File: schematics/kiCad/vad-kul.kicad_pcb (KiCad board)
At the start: 2 copper layers, 39 x 53.3 mm, 11 parts, among them J1 Lepton2Breakout, U1 RPIHeader

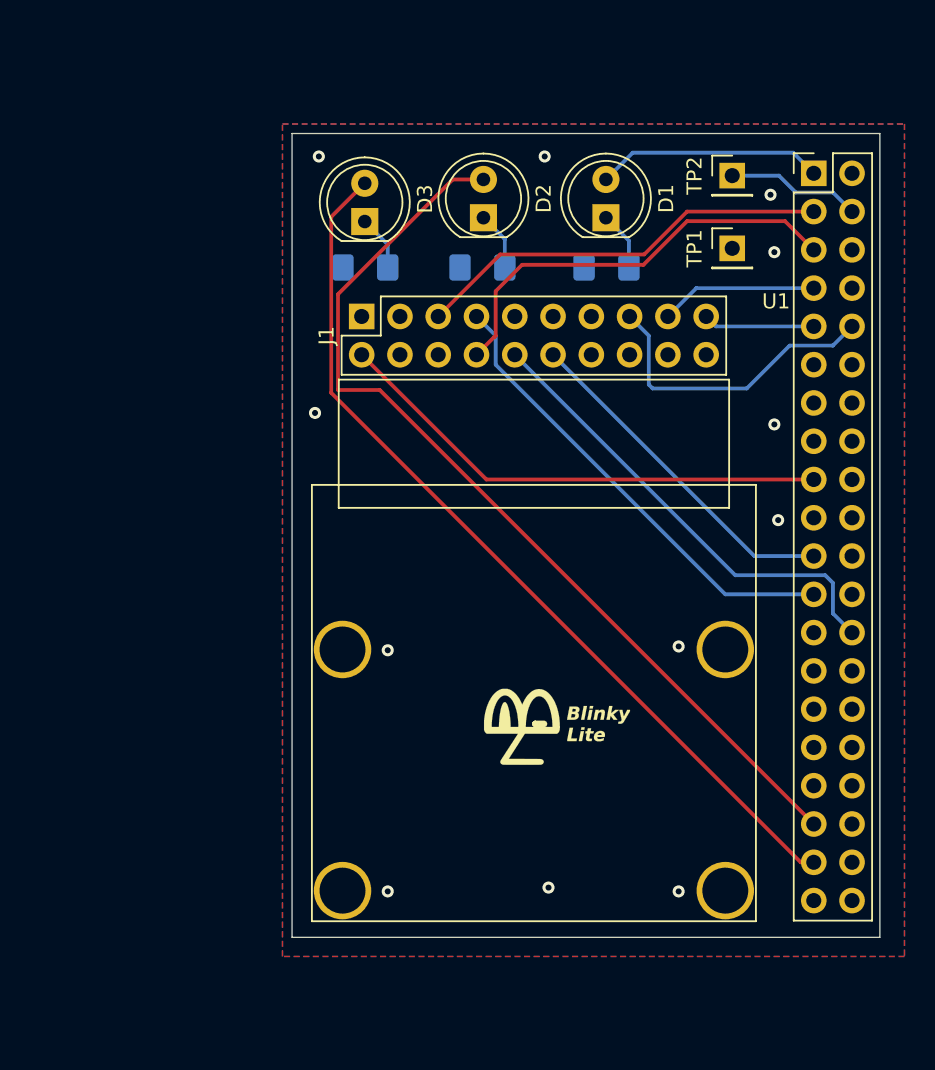
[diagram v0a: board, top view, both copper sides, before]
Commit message: new pcb with sr04
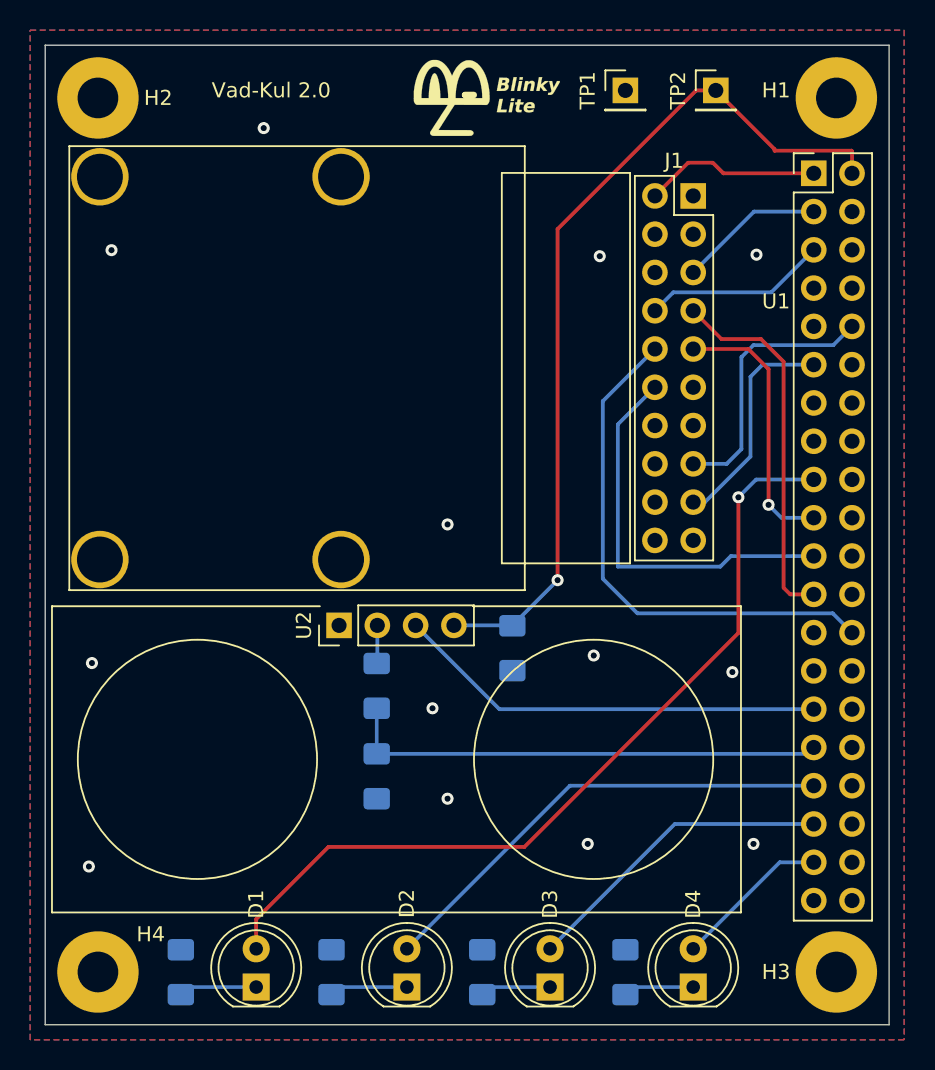
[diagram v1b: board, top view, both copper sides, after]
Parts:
- added C1: 1uF, Capacitor_SMD:C_1206_3216Metric_Pad1.42x1.75mm_HandSolder, B.Cu at (134.0, 57.0)
- added D4: LED, LED_THT:LED_D5.0mm, F.Cu at (146.0, 79.5)
- added H1: MountingHole_Pad, MountingHole:MountingHole_2.7mm_M2.5_Pad, F.Cu at (155.5, 20.5)
- added H2: MountingHole_Pad, MountingHole:MountingHole_2.7mm_M2.5_Pad, F.Cu at (106.5, 20.5)
- added H3: MountingHole_Pad, MountingHole:MountingHole_2.7mm_M2.5_Pad, F.Cu at (155.5, 78.5)
- added H4: MountingHole_Pad, MountingHole:MountingHole_2.7mm_M2.5_Pad, F.Cu at (106.5, 78.5)
- added R4: 220, Resistor_SMD:R_1206_3216Metric_Pad1.42x1.75mm_HandSolder, B.Cu at (141.5, 78.5)
- added R5: 3.3k, Resistor_SMD:R_1206_3216Metric_Pad1.42x1.75mm_HandSolder, B.Cu at (125.0, 59.5)
- added R6: 6.8k, Resistor_SMD:R_1206_3216Metric_Pad1.42x1.75mm_HandSolder, B.Cu at (125.0, 65.5)
- added U2: HC_SR04, dmcginnis427Footprints:HC_SR04, F.Cu at (122.5, 55.5)
- moved D1 56.1 mm to (117.0, 79.5)
- moved R1 54.6 mm to (112.0, 78.5), turned to 270 degrees
- moved D3 52.3 mm to (136.5, 79.5)
- moved D2 51.3 mm to (127.0, 79.5)
- moved R2 47.8 mm to (122.0, 78.5), turned to 270 degrees
- moved R3 47.4 mm to (132.0, 78.5), turned to 270 degrees
- moved G*** 42.0 mm to (132.5, 20.5)
- moved J1 23.4 mm to (146.0, 27.0), turned to 0 degrees
- moved TP1 12.7 mm to (141.5, 20.0)
- moved TP2 5.76 mm to (147.5, 20.0)
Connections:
- TP2 pad 1: Net-(TP2-Pad1) -> Net-(C1-Pad1)
- U1 pad 1: Net-(D1-Pad2) -> Net-(J1-Pad2)
- U1 pad 11: Net-(U1-Pad11) -> Net-(J1-Pad17)
- U1 pad 17: Net-(J1-Pad2) -> Net-(D1-Pad2)
- U1 pad 19: Net-(U1-Pad19) -> Net-(J1-Pad9)
- U1 pad 2: Net-(U1-Pad2) -> Net-(C1-Pad1)
- U1 pad 33: Net-(U1-Pad33) -> Net-(D2-Pad2)
- U1 pad 35: Net-(D2-Pad2) -> Net-(D3-Pad2)
- U1 pad 37: Net-(D3-Pad2) -> Net-(D4-Pad2)
- U1 pad 4: Net-(TP2-Pad1) -> Net-(U1-Pad4)
- U1 pad 7: Net-(J1-Pad17) -> Net-(U1-Pad7)
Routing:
- net Net-(C1-Pad1): track 0.00 -> 58.0 mm, vias 0 -> 1
- net Net-(D1-Pad2): track 15.1 -> 56.3 mm, vias 0 -> 1
- net Net-(D3-Pad2): track 59.8 -> 20.9 mm
- net Net-(R5-Pad2): track 0.00 -> 32.2 mm
- net Net-(D2-Pad2): track 62.7 -> 31.5 mm
- net Net-(U1-Pad29): track 0.00 -> 28.7 mm
- net Net-(J1-Pad2): track 33.4 -> 11.7 mm
- net Net-(J1-Pad5): track 27.8 -> 9.67 mm
- net Net-(J1-Pad9): track 0.00 -> 17.9 mm, vias 0 -> 1
- net Net-(J1-Pad8): track 28.6 -> 12.2 mm
- net Net-(D4-Pad2): track 0.00 -> 10.4 mm
- net Net-(TP2-Pad1): track 8.94 -> 0.00 mm
- net GND: track 7.41 -> 0.00 mm, vias 12 -> 13
- net Net-(J1-Pad7): track 31.1 -> 25.1 mm
- net Net-(D4-Pad1): track 0.00 -> 4.71 mm
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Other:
- board size 39 x 53.3 mm -> 56 x 65 mm
- board text added: "Vad-Kul 2.0"
